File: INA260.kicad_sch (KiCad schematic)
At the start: 2 parts, among them U1 INA260AIPWR

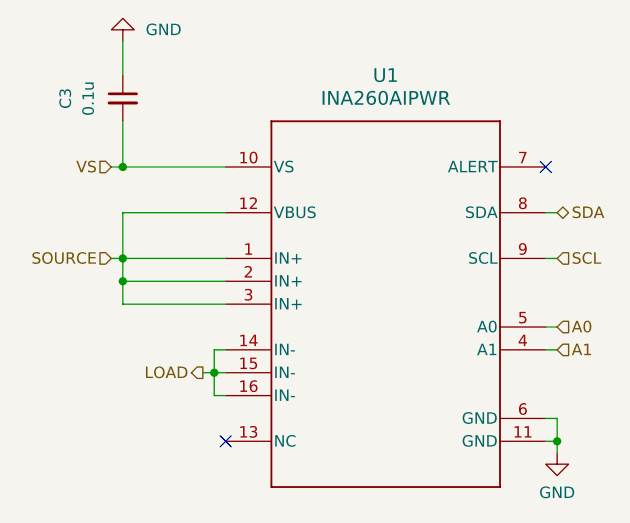
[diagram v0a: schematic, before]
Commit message: Start new PCB layout for second test article
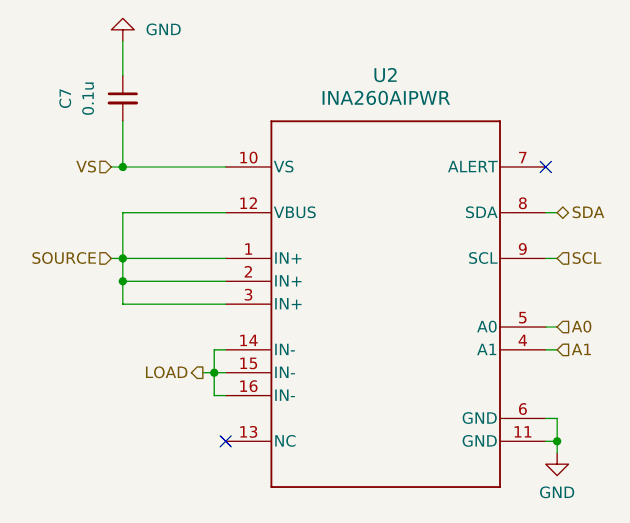
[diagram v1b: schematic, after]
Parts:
- renumbered C3 to C7, U1 to U2
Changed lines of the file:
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@@
 		(dnp no)
 		(fields_autoplaced yes)
-		(property "Reference" "C3"
+		(property "Reference" "C7"
 			(at 176.53 106.6864 90)
 			(effects
@@
 			(project "HEDGE2-OBC"
 				(path "/a13a6ce3-91ba-42e3-9b40-443fe6a0f2d9/740c0668-bfac-47e0-b7b8-de442260ca55"
-					(reference "C4")
+					(reference "C8")
 					(unit 1)
 				)
 				(path "/a13a6ce3-91ba-42e3-9b40-443fe6a0f2d9/9fa6cc5e-a76a-4d58-8af7-47af14171882"
-					(reference "C3")
+					(reference "C7")
 					(unit 1)
 				)
@@
 		(dnp no)
 		(fields_autoplaced yes)
-		(property "Reference" "#PWR041"
+		(property "Reference" "#PWR058"
 			(at 231.14 152.4 0)
 			(effects
@@
 			(project "HEDGE2-OBC"
 				(path "/a13a6ce3-91ba-42e3-9b40-443fe6a0f2d9/740c0668-bfac-47e0-b7b8-de442260ca55"
-					(reference "#PWR043")
+					(reference "#PWR060")
 					(unit 1)
 				)
 				(path "/a13a6ce3-91ba-42e3-9b40-443fe6a0f2d9/9fa6cc5e-a76a-4d58-8af7-47af14171882"
-					(reference "#PWR041")
+					(reference "#PWR058")
 					(unit 1)
 				)
@@
 		(dnp no)
 		(fields_autoplaced yes)
-		(property "Reference" "U1"
+		(property "Reference" "U2"
 			(at 212.09 104.14 0)
 			(effects
@@
 			(project "HEDGE2-OBC"
 				(path "/a13a6ce3-91ba-42e3-9b40-443fe6a0f2d9/740c0668-bfac-47e0-b7b8-de442260ca55"
+					(reference "U3")
+					(unit 1)
+				)
+				(path "/a13a6ce3-91ba-42e3-9b40-443fe6a0f2d9/9fa6cc5e-a76a-4d58-8af7-47af14171882"
 					(reference "U2")
-					(unit 1)
-				)
-				(path "/a13a6ce3-91ba-42e3-9b40-443fe6a0f2d9/9fa6cc5e-a76a-4d58-8af7-47af14171882"
-					(reference "U1")
 					(unit 1)
 				)
@@
 		(dnp no)
 		(fields_autoplaced yes)
-		(property "Reference" "#PWR040"
+		(property "Reference" "#PWR057"
 			(at 182.88 93.98 0)
 			(effects
@@
 			(project "HEDGE2-OBC"
 				(path "/a13a6ce3-91ba-42e3-9b40-443fe6a0f2d9/740c0668-bfac-47e0-b7b8-de442260ca55"
-					(reference "#PWR042")
+					(reference "#PWR059")
 					(unit 1)
 				)
 				(path "/a13a6ce3-91ba-42e3-9b40-443fe6a0f2d9/9fa6cc5e-a76a-4d58-8af7-47af14171882"
-					(reference "#PWR040")
-					(unit 1)
-				)
+					(reference "#PWR057")
+					(unit 1)
+				)

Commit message: Rework Novatel OEM719B symbol and footprint
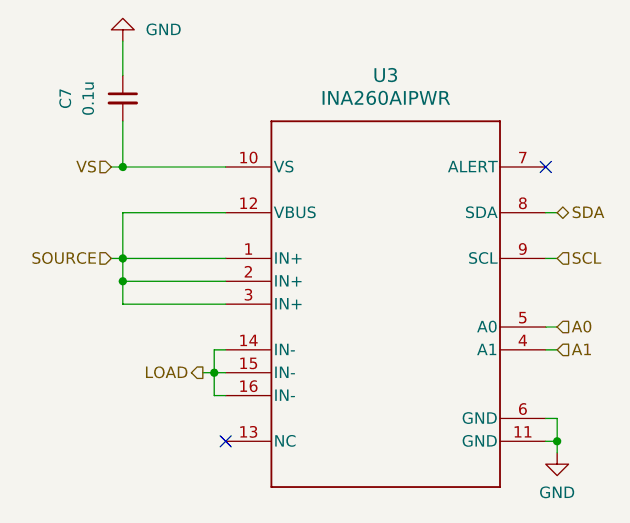
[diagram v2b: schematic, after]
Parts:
- renumbered U2 to U3
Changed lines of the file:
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@@
 		(dnp no)
 		(fields_autoplaced yes)
-		(property "Reference" "U2"
+		(property "Reference" "U3"
 			(at 212.09 104.14 0)
 			(effects
@@
 			(project "HEDGE2-OBC"
 				(path "/a13a6ce3-91ba-42e3-9b40-443fe6a0f2d9/740c0668-bfac-47e0-b7b8-de442260ca55"
+					(reference "U4")
+					(unit 1)
+				)
+				(path "/a13a6ce3-91ba-42e3-9b40-443fe6a0f2d9/9fa6cc5e-a76a-4d58-8af7-47af14171882"
 					(reference "U3")
 					(unit 1)
 				)
-				(path "/a13a6ce3-91ba-42e3-9b40-443fe6a0f2d9/9fa6cc5e-a76a-4d58-8af7-47af14171882"
-					(reference "U2")
-					(unit 1)
-				)

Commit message: Layout PCB; update footprints with 3D models
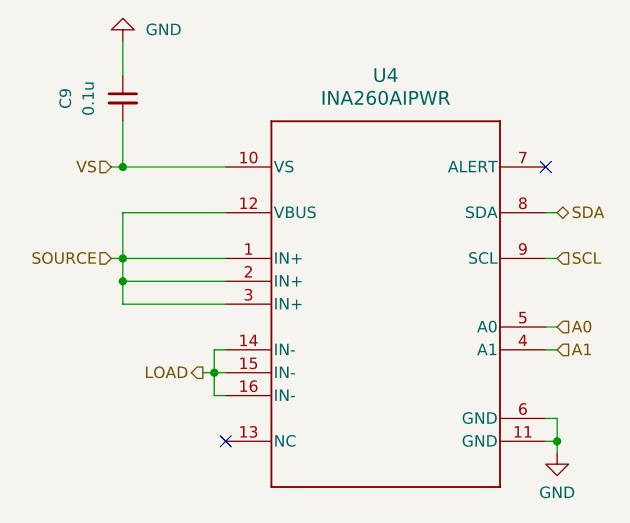
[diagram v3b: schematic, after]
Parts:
- renumbered C7 to C9, U3 to U4
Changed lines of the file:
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@@
 		(dnp no)
 		(fields_autoplaced yes)
-		(property "Reference" "C7"
+		(property "Reference" "C9"
 			(at 176.53 106.6864 90)
 			(effects
@@
 			(project "HEDGE2-OBC"
 				(path "/a13a6ce3-91ba-42e3-9b40-443fe6a0f2d9/740c0668-bfac-47e0-b7b8-de442260ca55"
-					(reference "C8")
+					(reference "C10")
 					(unit 1)
 				)
 				(path "/a13a6ce3-91ba-42e3-9b40-443fe6a0f2d9/9fa6cc5e-a76a-4d58-8af7-47af14171882"
-					(reference "C7")
+					(reference "C9")
 					(unit 1)
 				)
@@
 		(dnp no)
 		(fields_autoplaced yes)
-		(property "Reference" "#PWR058"
+		(property "Reference" "#PWR064"
 			(at 231.14 152.4 0)
 			(effects
@@
 			(project "HEDGE2-OBC"
 				(path "/a13a6ce3-91ba-42e3-9b40-443fe6a0f2d9/740c0668-bfac-47e0-b7b8-de442260ca55"
-					(reference "#PWR060")
+					(reference "#PWR066")
 					(unit 1)
 				)
 				(path "/a13a6ce3-91ba-42e3-9b40-443fe6a0f2d9/9fa6cc5e-a76a-4d58-8af7-47af14171882"
-					(reference "#PWR058")
+					(reference "#PWR064")
 					(unit 1)
 				)
@@
 		(dnp no)
 		(fields_autoplaced yes)
-		(property "Reference" "U3"
+		(property "Reference" "U4"
 			(at 212.09 104.14 0)
 			(effects
@@
 			(project "HEDGE2-OBC"
 				(path "/a13a6ce3-91ba-42e3-9b40-443fe6a0f2d9/740c0668-bfac-47e0-b7b8-de442260ca55"
+					(reference "U5")
+					(unit 1)
+				)
+				(path "/a13a6ce3-91ba-42e3-9b40-443fe6a0f2d9/9fa6cc5e-a76a-4d58-8af7-47af14171882"
 					(reference "U4")
-					(unit 1)
-				)
-				(path "/a13a6ce3-91ba-42e3-9b40-443fe6a0f2d9/9fa6cc5e-a76a-4d58-8af7-47af14171882"
-					(reference "U3")
 					(unit 1)
 				)
@@
 		(dnp no)
 		(fields_autoplaced yes)
-		(property "Reference" "#PWR057"
+		(property "Reference" "#PWR063"
 			(at 182.88 93.98 0)
 			(effects
@@
 			(project "HEDGE2-OBC"
 				(path "/a13a6ce3-91ba-42e3-9b40-443fe6a0f2d9/740c0668-bfac-47e0-b7b8-de442260ca55"
-					(reference "#PWR059")
+					(reference "#PWR065")
 					(unit 1)
 				)
 				(path "/a13a6ce3-91ba-42e3-9b40-443fe6a0f2d9/9fa6cc5e-a76a-4d58-8af7-47af14171882"
-					(reference "#PWR057")
-					(unit 1)
-				)
+					(reference "#PWR063")
+					(unit 1)
+				)

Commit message: Fix TCAN power supply swap
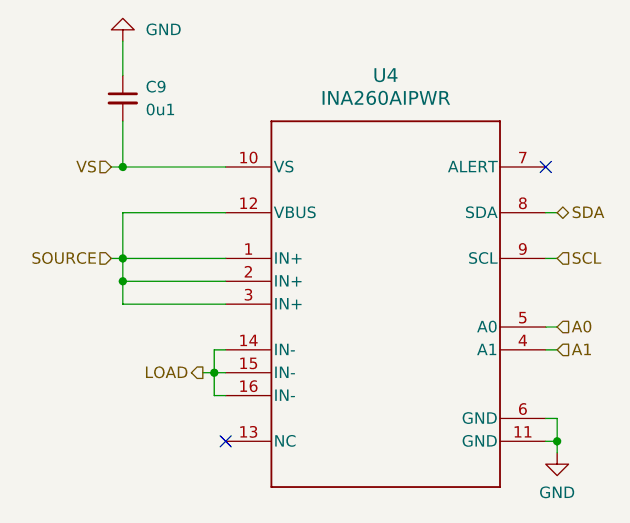
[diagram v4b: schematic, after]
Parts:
- C9: value 0.1u -> 0u1
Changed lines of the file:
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@@
 		(fields_autoplaced yes)
 		(property "Reference" "C9"
-			(at 176.53 106.6864 90)
+			(at 185.42 105.4162 0)
 			(effects
 				(font
 					(size 1.27 1.27)
 				)
+				(justify right)
 			)
 		)
-		(property "Value" "0.1u"
-			(at 179.07 106.6864 90)
+		(property "Value" "0u1"
+			(at 185.42 107.9562 0)
 			(effects
 				(font
 					(size 1.27 1.27)
 				)
+				(justify right)
 			)
 		)

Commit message: Add PCM5102A I2S audio output for APRS radio
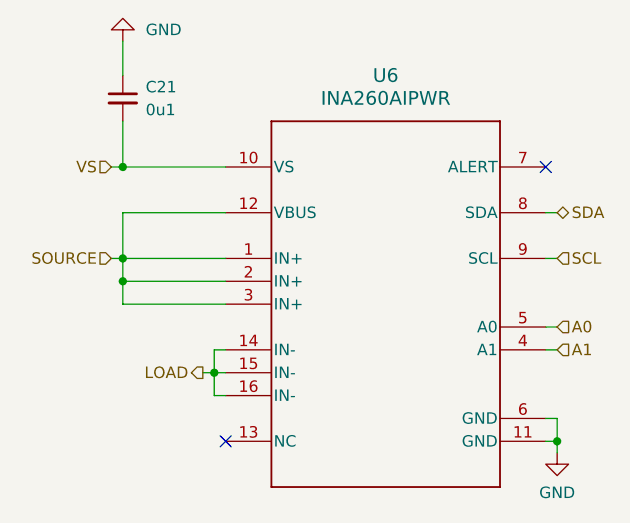
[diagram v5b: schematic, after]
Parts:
- renumbered C9 to C21, U4 to U6
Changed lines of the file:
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@@
 	(generator "eeschema")
 	(generator_version "9.0")
-	(paper "USLedger")
+	(paper "C")
 	(title_block
 		(title "HEDGE-2 OBC")
@@
 		(dnp no)
 		(fields_autoplaced yes)
-		(property "Reference" "C9"
+		(property "Reference" "C21"
 			(at 185.42 105.4162 0)
 			(effects
@@
 			(project "HEDGE2-OBC"
 				(path "/a13a6ce3-91ba-42e3-9b40-443fe6a0f2d9/740c0668-bfac-47e0-b7b8-de442260ca55"
-					(reference "C10")
+					(reference "C22")
 					(unit 1)
 				)
 				(path "/a13a6ce3-91ba-42e3-9b40-443fe6a0f2d9/9fa6cc5e-a76a-4d58-8af7-47af14171882"
-					(reference "C9")
+					(reference "C21")
 					(unit 1)
 				)
@@
 		(dnp no)
 		(fields_autoplaced yes)
-		(property "Reference" "#PWR064"
+		(property "Reference" "#PWR078"
 			(at 231.14 152.4 0)
 			(effects
@@
 			(project "HEDGE2-OBC"
 				(path "/a13a6ce3-91ba-42e3-9b40-443fe6a0f2d9/740c0668-bfac-47e0-b7b8-de442260ca55"
-					(reference "#PWR066")
+					(reference "#PWR080")
 					(unit 1)
 				)
 				(path "/a13a6ce3-91ba-42e3-9b40-443fe6a0f2d9/9fa6cc5e-a76a-4d58-8af7-47af14171882"
-					(reference "#PWR064")
+					(reference "#PWR078")
 					(unit 1)
 				)
@@
 		(dnp no)
 		(fields_autoplaced yes)
-		(property "Reference" "U4"
+		(property "Reference" "U6"
 			(at 212.09 104.14 0)
 			(effects
@@
 			(project "HEDGE2-OBC"
 				(path "/a13a6ce3-91ba-42e3-9b40-443fe6a0f2d9/740c0668-bfac-47e0-b7b8-de442260ca55"
-					(reference "U5")
+					(reference "U7")
 					(unit 1)
 				)
 				(path "/a13a6ce3-91ba-42e3-9b40-443fe6a0f2d9/9fa6cc5e-a76a-4d58-8af7-47af14171882"
-					(reference "U4")
+					(reference "U6")
 					(unit 1)
 				)
@@
 		(dnp no)
 		(fields_autoplaced yes)
-		(property "Reference" "#PWR063"
+		(property "Reference" "#PWR077"
 			(at 182.88 93.98 0)
 			(effects
@@
 			(project "HEDGE2-OBC"
 				(path "/a13a6ce3-91ba-42e3-9b40-443fe6a0f2d9/740c0668-bfac-47e0-b7b8-de442260ca55"
-					(reference "#PWR065")
+					(reference "#PWR079")
 					(unit 1)
 				)
 				(path "/a13a6ce3-91ba-42e3-9b40-443fe6a0f2d9/9fa6cc5e-a76a-4d58-8af7-47af14171882"
-					(reference "#PWR063")
+					(reference "#PWR077")
 					(unit 1)
 				)

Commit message: Add PCM and SPI UART; begin layout update
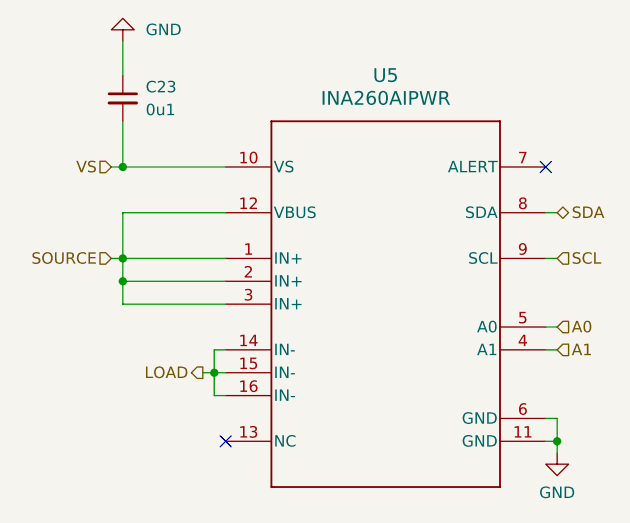
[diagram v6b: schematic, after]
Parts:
- renumbered C21 to C23, U6 to U5
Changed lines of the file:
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@@
 		(dnp no)
 		(fields_autoplaced yes)
-		(property "Reference" "C21"
+		(property "Reference" "C23"
 			(at 185.42 105.4162 0)
 			(effects
@@
 			(project "HEDGE2-OBC"
 				(path "/a13a6ce3-91ba-42e3-9b40-443fe6a0f2d9/740c0668-bfac-47e0-b7b8-de442260ca55"
-					(reference "C22")
+					(reference "C24")
 					(unit 1)
 				)
 				(path "/a13a6ce3-91ba-42e3-9b40-443fe6a0f2d9/9fa6cc5e-a76a-4d58-8af7-47af14171882"
-					(reference "C21")
+					(reference "C23")
 					(unit 1)
 				)
@@
 		(dnp no)
 		(fields_autoplaced yes)
-		(property "Reference" "#PWR078"
+		(property "Reference" "#PWR079"
 			(at 231.14 152.4 0)
 			(effects
@@
 			(project "HEDGE2-OBC"
 				(path "/a13a6ce3-91ba-42e3-9b40-443fe6a0f2d9/740c0668-bfac-47e0-b7b8-de442260ca55"
-					(reference "#PWR080")
+					(reference "#PWR081")
 					(unit 1)
 				)
 				(path "/a13a6ce3-91ba-42e3-9b40-443fe6a0f2d9/9fa6cc5e-a76a-4d58-8af7-47af14171882"
-					(reference "#PWR078")
+					(reference "#PWR079")
 					(unit 1)
 				)
@@
 		(dnp no)
 		(fields_autoplaced yes)
-		(property "Reference" "U6"
+		(property "Reference" "U5"
 			(at 212.09 104.14 0)
 			(effects
@@
 			(project "HEDGE2-OBC"
 				(path "/a13a6ce3-91ba-42e3-9b40-443fe6a0f2d9/740c0668-bfac-47e0-b7b8-de442260ca55"
-					(reference "U7")
+					(reference "U6")
 					(unit 1)
 				)
 				(path "/a13a6ce3-91ba-42e3-9b40-443fe6a0f2d9/9fa6cc5e-a76a-4d58-8af7-47af14171882"
-					(reference "U6")
+					(reference "U5")
 					(unit 1)
 				)
@@
 		(dnp no)
 		(fields_autoplaced yes)
-		(property "Reference" "#PWR077"
+		(property "Reference" "#PWR078"
 			(at 182.88 93.98 0)
 			(effects
@@
 			(project "HEDGE2-OBC"
 				(path "/a13a6ce3-91ba-42e3-9b40-443fe6a0f2d9/740c0668-bfac-47e0-b7b8-de442260ca55"
-					(reference "#PWR079")
+					(reference "#PWR080")
 					(unit 1)
 				)
 				(path "/a13a6ce3-91ba-42e3-9b40-443fe6a0f2d9/9fa6cc5e-a76a-4d58-8af7-47af14171882"
-					(reference "#PWR077")
-					(unit 1)
-				)
+					(reference "#PWR078")
+					(unit 1)
+				)

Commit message: Continue layout update
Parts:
- renumbered C23 to C22
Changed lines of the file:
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@@
 		(dnp no)
 		(fields_autoplaced yes)
-		(property "Reference" "C23"
+		(property "Reference" "C22"
 			(at 185.42 105.4162 0)
 			(effects
@@
 			(project "HEDGE2-OBC"
 				(path "/a13a6ce3-91ba-42e3-9b40-443fe6a0f2d9/740c0668-bfac-47e0-b7b8-de442260ca55"
-					(reference "C24")
+					(reference "C23")
 					(unit 1)
 				)
 				(path "/a13a6ce3-91ba-42e3-9b40-443fe6a0f2d9/9fa6cc5e-a76a-4d58-8af7-47af14171882"
-					(reference "C23")
+					(reference "C22")
 					(unit 1)
 				)
@@
 		(dnp no)
 		(fields_autoplaced yes)
-		(property "Reference" "#PWR079"
+		(property "Reference" "#PWR085"
 			(at 231.14 152.4 0)
 			(effects
@@
 			(project "HEDGE2-OBC"
 				(path "/a13a6ce3-91ba-42e3-9b40-443fe6a0f2d9/740c0668-bfac-47e0-b7b8-de442260ca55"
-					(reference "#PWR081")
+					(reference "#PWR087")
 					(unit 1)
 				)
 				(path "/a13a6ce3-91ba-42e3-9b40-443fe6a0f2d9/9fa6cc5e-a76a-4d58-8af7-47af14171882"
-					(reference "#PWR079")
+					(reference "#PWR085")
 					(unit 1)
 				)
@@
 		(dnp no)
 		(fields_autoplaced yes)
-		(property "Reference" "#PWR078"
+		(property "Reference" "#PWR084"
 			(at 182.88 93.98 0)
 			(effects
@@
 			(project "HEDGE2-OBC"
 				(path "/a13a6ce3-91ba-42e3-9b40-443fe6a0f2d9/740c0668-bfac-47e0-b7b8-de442260ca55"
-					(reference "#PWR080")
+					(reference "#PWR086")
 					(unit 1)
 				)
 				(path "/a13a6ce3-91ba-42e3-9b40-443fe6a0f2d9/9fa6cc5e-a76a-4d58-8af7-47af14171882"
-					(reference "#PWR078")
-					(unit 1)
-				)
+					(reference "#PWR084")
+					(unit 1)
+				)

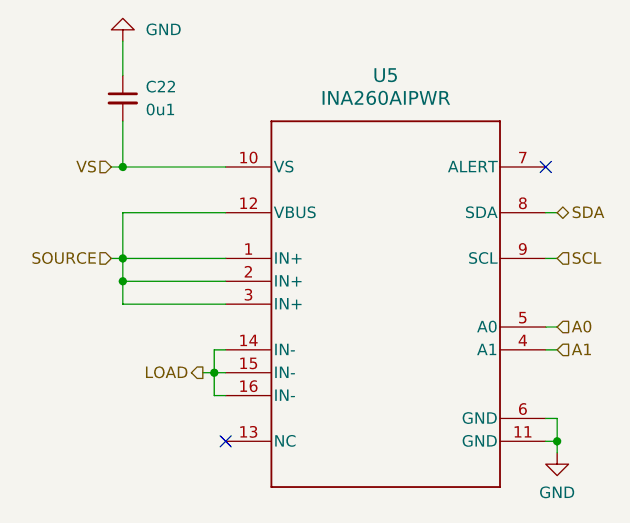
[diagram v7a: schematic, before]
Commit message: Add IMU; eliminate environmental sensor; finish layout
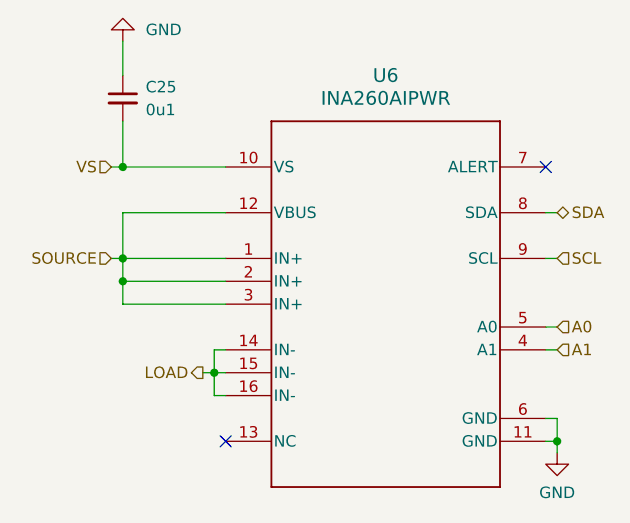
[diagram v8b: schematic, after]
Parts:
- renumbered C22 to C25, U5 to U6
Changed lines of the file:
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@@
 		(dnp no)
 		(fields_autoplaced yes)
-		(property "Reference" "C22"
+		(property "Reference" "C25"
 			(at 185.42 105.4162 0)
 			(effects
@@
 		(property "SNAPEDA_PN" ""
 			(at 182.88 106.68 90)
+			(effects
+				(font
+					(size 1.27 1.27)
+				)
+				(hide yes)
+			)
+		)
+		(property "Availability" ""
+			(at 182.88 106.68 0)
+			(effects
+				(font
+					(size 1.27 1.27)
+				)
+				(hide yes)
+			)
+		)
+		(property "Price" ""
+			(at 182.88 106.68 0)
 			(effects
 				(font
@@
 			(project "HEDGE2-OBC"
 				(path "/a13a6ce3-91ba-42e3-9b40-443fe6a0f2d9/740c0668-bfac-47e0-b7b8-de442260ca55"
-					(reference "C23")
+					(reference "C26")
 					(unit 1)
 				)
 				(path "/a13a6ce3-91ba-42e3-9b40-443fe6a0f2d9/9fa6cc5e-a76a-4d58-8af7-47af14171882"
-					(reference "C22")
+					(reference "C25")
 					(unit 1)
 				)
@@
 		(dnp no)
 		(fields_autoplaced yes)
-		(property "Reference" "#PWR085"
+		(property "Reference" "#PWR093"
 			(at 231.14 152.4 0)
 			(effects
@@
 			(project "HEDGE2-OBC"
 				(path "/a13a6ce3-91ba-42e3-9b40-443fe6a0f2d9/740c0668-bfac-47e0-b7b8-de442260ca55"
-					(reference "#PWR087")
+					(reference "#PWR095")
 					(unit 1)
 				)
 				(path "/a13a6ce3-91ba-42e3-9b40-443fe6a0f2d9/9fa6cc5e-a76a-4d58-8af7-47af14171882"
-					(reference "#PWR085")
+					(reference "#PWR093")
 					(unit 1)
 				)
@@
 		(dnp no)
 		(fields_autoplaced yes)
-		(property "Reference" "U5"
+		(property "Reference" "U6"
 			(at 212.09 104.14 0)
 			(effects
@@
 		)
 		(property "SNAPEDA_PN" ""
+			(at 212.09 129.54 0)
+			(effects
+				(font
+					(size 1.27 1.27)
+				)
+				(hide yes)
+			)
+		)
+		(property "Availability" ""
+			(at 212.09 129.54 0)
+			(effects
+				(font
+					(size 1.27 1.27)
+				)
+				(hide yes)
+			)
+		)
+		(property "Price" ""
 			(at 212.09 129.54 0)
 			(effects
@@
 			(project "HEDGE2-OBC"
 				(path "/a13a6ce3-91ba-42e3-9b40-443fe6a0f2d9/740c0668-bfac-47e0-b7b8-de442260ca55"
+					(reference "U7")
+					(unit 1)
+				)
+				(path "/a13a6ce3-91ba-42e3-9b40-443fe6a0f2d9/9fa6cc5e-a76a-4d58-8af7-47af14171882"
 					(reference "U6")
-					(unit 1)
-				)
-				(path "/a13a6ce3-91ba-42e3-9b40-443fe6a0f2d9/9fa6cc5e-a76a-4d58-8af7-47af14171882"
-					(reference "U5")
 					(unit 1)
 				)
@@
 		(dnp no)
 		(fields_autoplaced yes)
-		(property "Reference" "#PWR084"
+		(property "Reference" "#PWR092"
 			(at 182.88 93.98 0)
 			(effects
@@
 			(project "HEDGE2-OBC"
 				(path "/a13a6ce3-91ba-42e3-9b40-443fe6a0f2d9/740c0668-bfac-47e0-b7b8-de442260ca55"
-					(reference "#PWR086")
+					(reference "#PWR094")
 					(unit 1)
 				)
 				(path "/a13a6ce3-91ba-42e3-9b40-443fe6a0f2d9/9fa6cc5e-a76a-4d58-8af7-47af14171882"
-					(reference "#PWR084")
-					(unit 1)
-				)
+					(reference "#PWR092")
+					(unit 1)
+				)
